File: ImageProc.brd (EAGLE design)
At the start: 49.8 x 23.2 mm, 119 parts, among them IC1 XC61GC3002HR-G, IC10 AT45DB642D-CNU, IC2 MIC5335-SPYMT, IC3 MIC5335-JGYMT, IC4 DSPIC33FJ128MC706A, IC5 AT86RF233-ZU, IC6 LTC6088, IC7 DRV8833RTY, IC8 DRV8833RTY, IC9 MPU-6000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

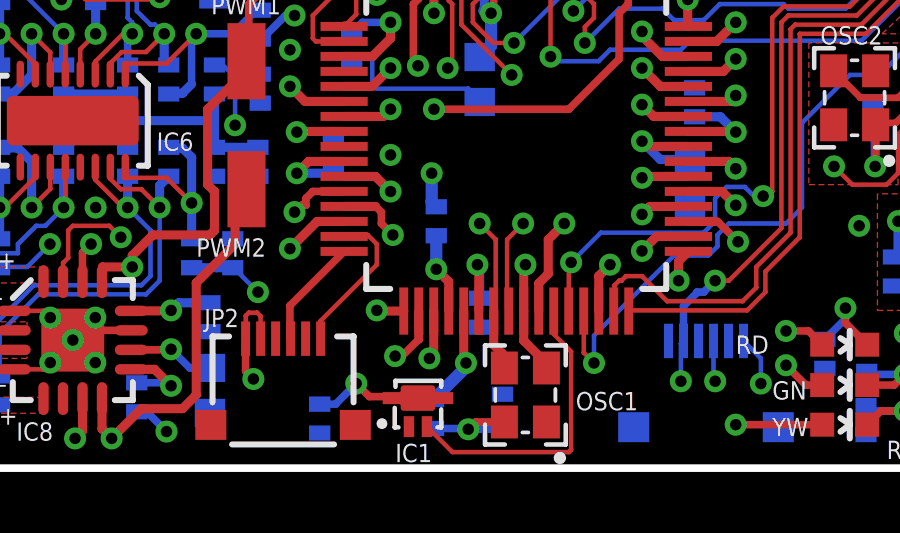
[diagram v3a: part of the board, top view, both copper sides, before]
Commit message: Fix transposed SDA1/SCL1 on dsPIC
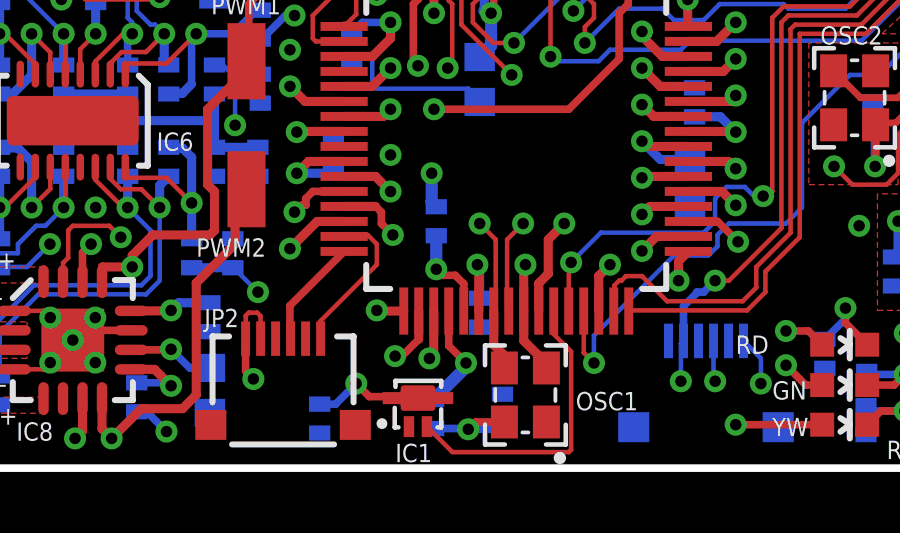
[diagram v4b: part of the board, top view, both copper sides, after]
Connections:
- net SCL1: now also IC4.37; no longer IC4.36
- net SDA1: now also IC4.36; no longer IC4.37
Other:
- board text added: "2012.10.23"
- board text added: "ImageProc 2.5 Rev. C"
- board text removed: "2012.08.18"
- board text removed: "ImageProc 2.5 Rev. B"
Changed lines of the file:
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@@
 <grid distance="1" unitdist="mil" unit="mil" style="lines" multiple="1" display="yes" altdistance="1" altunitdist="mil" altunit="mil"/>
 <layers>
-<layer number="1" name="Top" color="4" fill="1" visible="yes" active="yes"/>
+<layer number="1" name="Top" color="4" fill="1" visible="no" active="yes"/>
 <layer number="2" name="Ground" color="2" fill="1" visible="no" active="yes"/>
 <layer number="3" name="Power" color="5" fill="1" visible="no" active="yes"/>
@@
 <layer number="20" name="Dimension" color="15" fill="1" visible="no" active="yes"/>
 <layer number="21" name="tPlace" color="16" fill="1" visible="no" active="yes"/>
-<layer number="22" name="bPlace" color="14" fill="1" visible="no" active="yes"/>
+<layer number="22" name="bPlace" color="14" fill="1" visible="yes" active="yes"/>
 <layer number="23" name="tOrigins" color="15" fill="1" visible="no" active="yes"/>
 <layer number="24" name="bOrigins" color="15" fill="1" visible="no" active="yes"/>
@@
 <layer number="27" name="tValues" color="7" fill="1" visible="yes" active="yes"/>
 <layer number="28" name="bValues" color="7" fill="1" visible="yes" active="yes"/>
-<layer number="29" name="tStop" color="7" fill="3" visible="yes" active="yes"/>
+<layer number="29" name="tStop" color="7" fill="3" visible="no" active="yes"/>
 <layer number="30" name="bStop" color="7" fill="6" visible="no" active="yes"/>
 <layer number="31" name="tCream" color="7" fill="4" visible="no" active="yes"/>
@@
 <layer number="37" name="tTest" color="7" fill="1" visible="no" active="yes"/>
 <layer number="38" name="bTest" color="7" fill="1" visible="no" active="yes"/>
-<layer number="39" name="tKeepout" color="4" fill="11" visible="yes" active="yes"/>
+<layer number="39" name="tKeepout" color="4" fill="11" visible="no" active="yes"/>
 <layer number="40" name="bKeepout" color="1" fill="11" visible="no" active="yes"/>
 <layer number="41" name="tRestrict" color="4" fill="10" visible="yes" active="yes"/>
@@
 <text x="49.370025" y="5.628090625" size="0.6096" layer="22" font="vector" ratio="25" rot="MR0">Douglas Hutchings</text>
 <text x="49.3776" y="6.5532" size="0.6096" layer="22" font="vector" ratio="25" rot="MR0">Ryan Julian</text>
-<text x="49.3776" y="1.3716" size="0.6096" layer="22" font="vector" ratio="25" rot="MR0">2012.08.18</text>
-<text x="49.3776" y="0.4572" size="0.6096" layer="22" font="vector" ratio="25" rot="MR0">ImageProc 2.5 Rev. B</text>
+<text x="49.3776" y="1.3716" size="0.6096" layer="22" font="vector" ratio="25" rot="MR0">2012.10.23</text>
+<text x="49.3776" y="0.4572" size="0.6096" layer="22" font="vector" ratio="25" rot="MR0">ImageProc 2.5 Rev. C</text>
 <text x="49.3776" y="4.4196" size="0.6096" layer="22" font="vector" ratio="25" rot="MR0">Biomimetic</text>
 <text x="49.3776" y="3.5052" size="0.6096" layer="22" font="vector" ratio="25" rot="MR0">Millisystems</text>
@@
 design rules under a new name.</description>
 <param name="layerSetup" value="(1*2+3*16)"/>
-<param name="mtCopper" value="0.035559375mm 0.035559375mm 0.035559375mm 0.0356mm 0.0356mm 0.0356mm 0.0356mm 0.0356mm 0.0356mm 0.0356mm 0.0356mm 0.0356mm 0.0356mm 0.0356mm 0.0356mm 0.035559375mm"/>
+<param name="mtCopper" value="2mil 2mil 2mil 0.0356mm 0.0356mm 0.0356mm 0.0356mm 0.0356mm 0.0356mm 0.0356mm 0.0356mm 0.0356mm 0.0356mm 0.0356mm 0.0356mm 2mil"/>
 <param name="mtIsolate" value="9mil 40mil 9mil 0.1499mm 0.2007mm 0.1499mm 0.2007mm 0.1499mm 0.2007mm 0.1499mm 0.2007mm 0.1499mm 0.2007mm 0.1499mm 0.2007mm"/>
 <param name="mdWireWire" value="6mil"/>
@@
 <contactref element="R4" pad="1"/>
 <contactref element="JP3" pad="3"/>
-<contactref element="IC4" pad="36"/>
+<contactref element="IC4" pad="37"/>
 <via x="48.387" y="18.4404" extent="1-16" drill="0.381"/>
 <wire x1="45.5214" y1="17.7708" x2="46.3458" y2="17.7708" width="0.1524" layer="1"/>
@@
 <wire x1="47.0154" y1="18.4404" x2="48.387" y2="18.4404" width="0.1524" layer="1"/>
 <via x="20.0406" y="6.6294" extent="1-16" drill="0.381"/>
-<wire x1="20.0406" y1="6.6294" x2="20.4576" y2="6.2124" width="0.3048" layer="1"/>
-<wire x1="20.4576" y1="6.2124" x2="20.4576" y2="5.2353" width="0.3048" layer="1"/>
 <wire x1="20.0406" y1="7.747" x2="20.0406" y2="6.6294" width="0.4064" layer="16"/>
 <via x="29.337" y="2.8956" extent="1-16" drill="0.381"/>
@@
 <wire x1="29.2822" y1="3.1028" x2="29.337" y2="3.048" width="0.1524" layer="16"/>
 <wire x1="29.337" y1="3.048" x2="29.337" y2="2.8956" width="0.1524" layer="16"/>
+<wire x1="20.9576" y1="5.2353" x2="20.9576" y2="6.1442" width="0.254" layer="1"/>
+<wire x1="20.9576" y1="6.1442" x2="20.6756" y2="6.4262" width="0.254" layer="1"/>
+<wire x1="20.6756" y1="6.4262" x2="20.2438" y2="6.4262" width="0.254" layer="1"/>
+<wire x1="20.2438" y1="6.4262" x2="20.0406" y2="6.6294" width="0.254" layer="1"/>
 </signal>
 <signal name="SDA1">
@@
 <contactref element="R5" pad="1"/>
 <contactref element="JP3" pad="5"/>
-<contactref element="IC4" pad="37"/>
+<contactref element="IC4" pad="36"/>
 <via x="48.387" y="19.812" extent="1-16" drill="0.381"/>
 <wire x1="45.5214" y1="18.7708" x2="45.9742" y2="18.7708" width="0.1524" layer="1"/>
@@
 <via x="21.0312" y="3.5052" extent="1-16" drill="0.381"/>
 <wire x1="21.0312" y1="3.5052" x2="20.9576" y2="3.5788" width="0.3048" layer="1"/>
-<wire x1="20.9576" y1="3.5788" x2="20.9576" y2="5.2353" width="0.3048" layer="1"/>
 <wire x1="48.4632" y1="19.812" x2="48.387" y2="19.812" width="0.1524" layer="3"/>
 <wire x1="19.9517" y1="2.286" x2="21.0312" y2="3.3655" width="0.4064" layer="16"/>
@@
 <wire x1="28.2822" y1="5.3982" x2="28.7274" y2="5.8434" width="0.254" layer="16"/>
 <wire x1="28.7274" y1="5.8434" x2="28.7274" y2="5.8674" width="0.254" layer="16"/>
+<wire x1="20.9576" y1="3.5788" x2="20.4576" y2="4.0788" width="0.254" layer="1"/>
+<wire x1="20.4576" y1="4.0788" x2="20.4576" y2="5.2353" width="0.254" layer="1"/>
 </signal>
 <signal name="SDO2">
